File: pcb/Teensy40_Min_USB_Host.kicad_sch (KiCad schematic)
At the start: 11 parts, among them J1 USB_A, J2 Conn_01x14, J3 Conn_01x14, U1 TPD3S014, U2 Teensy4.0

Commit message: Change fuse footprint
Use the proper 0805 fuse footprint instead of the 0805 inductor footprint.
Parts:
- F1: footprint Inductor_SMD:L_0805_2012Metric -> Fuse:Fuse_0805_2012Metric
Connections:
- net at U2.3V3: now also J3.3 (Pin_3)
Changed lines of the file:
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@@
     (property "Reference" "F1" (id 0) (at 161.29 101.3165 90))
     (property "Value" "500 mA" (id 1) (at 161.29 104.0916 90))
-    (property "Footprint" "Inductor_SMD:L_0805_2012Metric" (id 2) (at 166.37 105.41 0)
+    (property "Footprint" "Fuse:Fuse_0805_2012Metric" (id 2) (at 166.37 105.41 0)
       (effects (font (size 1.27 1.27)) (justify left) hide)
     )
@@
     )
     (path "/f5825cc6-95a9-4e27-8336-4f8229fc1924"
-      (reference "F1") (unit 1) (value "500 mA") (footprint "Inductor_SMD:L_0805_2012Metric")
+      (reference "F1") (unit 1) (value "500 mA") (footprint "Fuse:Fuse_0805_2012Metric")
     )
     (path "/9ae6e37b-e62d-471c-bde9-8fd51e595ee6"

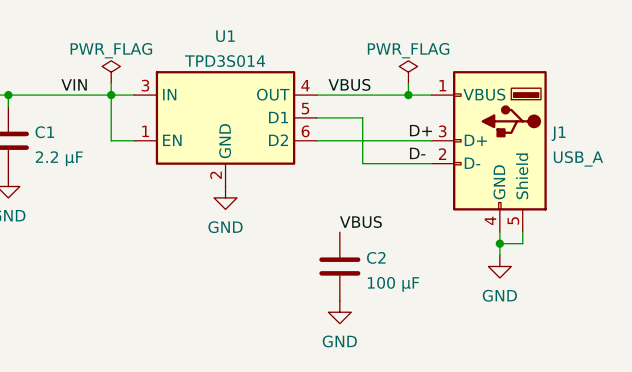
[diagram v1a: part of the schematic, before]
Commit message: Replace C2 cap with tantalum, 150 uF
Having some suspected brownout issues with rumble motors using the 100 uF ceramic cap, and I found some documentation from TI that says the USB host output capacitance should be 120 µF at a minimum.
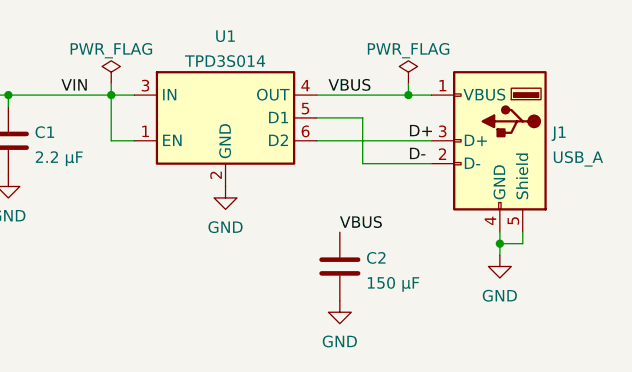
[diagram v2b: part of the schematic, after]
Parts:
- C2: value 100 µF -> 150 µF; footprint Capacitor_SMD:C_1206_3216Metric -> Capacitor_Tantalum_SMD:CP_EIA-3216-10_Kemet-I; DigiKey Product Number 13-CC1206MKX5R5BB107CT-ND -> 478-6250-1-ND; Manufacturer YAGEO -> KYOCERA AVX; Manufacturer Product Number CC1206MKX5R5BB107 -> TLNK157M006R2500
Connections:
- net at U2.3V3: now also J3.3 (Pin_3)
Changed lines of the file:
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@@
       (effects (font (size 1.27 1.27)) (justify left))
     )
-    (property "Value" "100 µF" (id 1) (at 221.361 127.5966 0)
+    (property "Value" "150 µF" (id 1) (at 221.361 127.5966 0)
       (effects (font (size 1.27 1.27)) (justify left))
     )
-    (property "Footprint" "Capacitor_SMD:C_1206_3216Metric" (id 2) (at 219.4052 129.54 0)
+    (property "Footprint" "Capacitor_Tantalum_SMD:CP_EIA-3216-10_Kemet-I" (id 2) (at 219.4052 129.54 0)
       (effects (font (size 1.27 1.27)) hide)
     )
-    (property "Datasheet" "https://www.yageo.com/upload/media/product/productsearch/datasheet/mlcc/UPY-GPHC_X5R_4V-to-50V_26.pdf" (id 3) (at 218.44 125.73 0)
+    (property "Datasheet" "https://datasheets.kyocera-avx.com/TLN_Undertab.pdf" (id 3) (at 218.44 125.73 0)
       (effects (font (size 1.27 1.27)) hide)
     )
-    (property "Description" "CAP CER 100UF 6.3V X5R 1206" (id 4) (at 218.44 125.73 0)
+    (property "Description" "CAP TANT 150UF 20% 6.3V 1206" (id 4) (at 218.44 125.73 0)
       (effects (font (size 1.27 1.27)) hide)
     )
-    (property "DigiKey Product Number" "13-CC1206MKX5R5BB107CT-ND" (id 5) (at 218.44 125.73 0)
+    (property "DigiKey Product Number" "478-6250-1-ND" (id 5) (at 218.44 125.73 0)
       (effects (font (size 1.27 1.27)) hide)
     )
-    (property "Manufacturer" "YAGEO" (id 6) (at 218.44 125.73 0)
+    (property "Manufacturer" "KYOCERA AVX" (id 6) (at 218.44 125.73 0)
       (effects (font (size 1.27 1.27)) hide)
     )
-    (property "Manufacturer Product Number" "CC1206MKX5R5BB107" (id 7) (at 218.44 125.73 0)
+    (property "Manufacturer Product Number" "TLNK157M006R2500" (id 7) (at 218.44 125.73 0)
       (effects (font (size 1.27 1.27)) hide)
     )
@@
     )
     (path "/eb66ee31-9e4d-4772-a4e6-76ee3a23c3dc"
-      (reference "C2") (unit 1) (value "100 µF") (footprint "Capacitor_SMD:C_1206_3216Metric")
+      (reference "C2") (unit 1) (value "150 µF") (footprint "Capacitor_Tantalum_SMD:CP_EIA-3216-10_Kemet-I")
     )
     (path "/f5825cc6-95a9-4e27-8336-4f8229fc1924"

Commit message: Update Teensy schematic symbol from lib
I forgot to update the schematic after updating the library. Committing now to satisfy the ERC check.
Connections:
- net at U2.3V3: now also J3.3 (Pin_3)

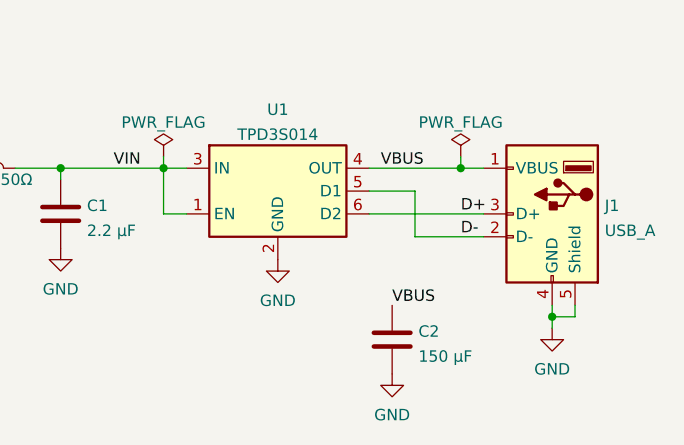
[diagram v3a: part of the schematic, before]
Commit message: Add VBUS label to schematic
Better than using a local label standalone.
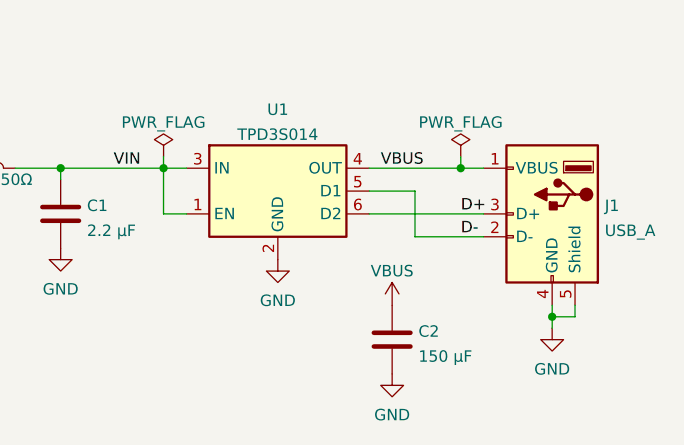
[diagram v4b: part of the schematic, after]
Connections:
- net at U2.3V3: now also J3.3 (Pin_3)
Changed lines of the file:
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@@
-    (effects (font (size 1.27 1.27)) (justify left bottom))
-  )
-  (label "VBUS" (at 218.44 121.92 0)
     (effects (font (size 1.27 1.27)) (justify left bottom))
   )
@@
     )
     (property "Datasheet" "" (id 3) (at 43.18 60.96 0)
+      (effects (font (size 1.27 1.27)) hide)
+    )
+    (pin "1")
+  )
+  (symbol (lib_id "power:VBUS") (at 218.44 121.92 0) (unit 1)
+    (in_bom yes) (on_board yes)
+    (property "Reference" "#PWR0111" (id 0) (at 218.44 125.73 0)
+      (effects (font (size 1.27 1.27)) hide)
+    )
+    (property "Value" "VBUS" (id 1) (at 218.44 118.11 0))
+    (property "Footprint" "" (id 2) (at 218.44 121.92 0)
+      (effects (font (size 1.27 1.27)) hide)
+    )
+    (property "Datasheet" "" (id 3) (at 218.44 121.92 0)
       (effects (font (size 1.27 1.27)) hide)
     )
@@
       (reference "#PWR0110") (unit 1) (value "GND") (footprint "")
     )
+    (path "/293a4c55-6604-4fbb-9af9-66b46d725551"
+      (reference "#PWR0111") (unit 1) (value "VBUS") (footprint "")
+    )
     (path "/0359c70a-e44f-4e0f-8034-bf0207c3516a"

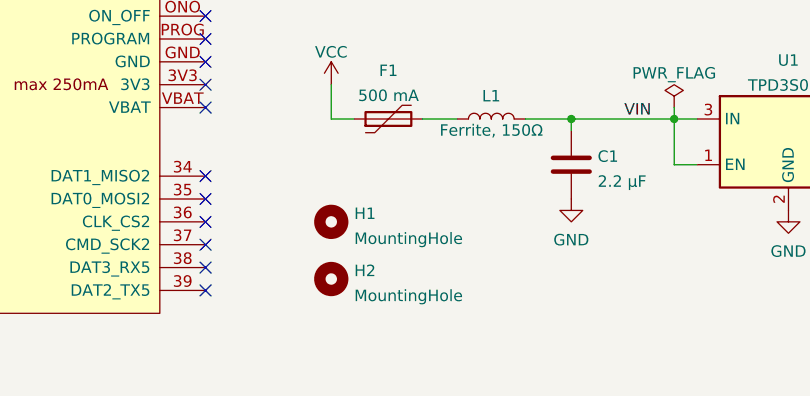
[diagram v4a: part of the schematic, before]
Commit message: Remove H2 mounting hole
This semi-circle is now part of the board outline, and the radius (1.6 mm) is large enough for most board houses that a separate drill is not needed.
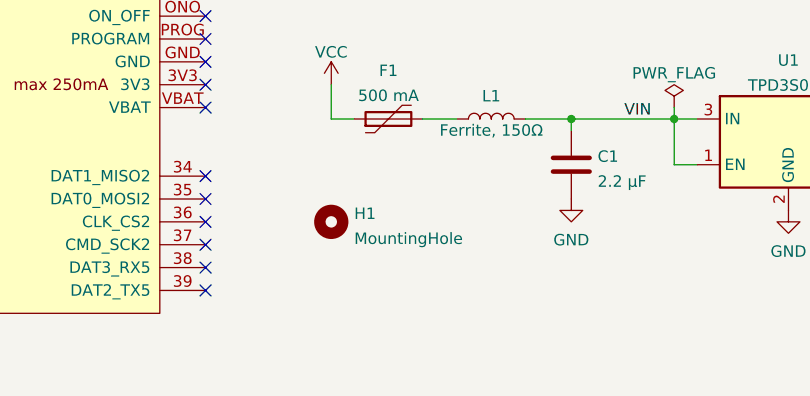
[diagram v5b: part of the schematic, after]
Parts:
- removed H2: MountingHole, Teensy40_Min_USB_Host:MountingHole_3.2mm, symbol Mechanical:MountingHole
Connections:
- net at U2.3V3: now also J3.3 (Pin_3)
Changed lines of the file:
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@@
     (pin "9")
-  )
-  (symbol (lib_id "Mechanical:MountingHole") (at 154.94 124.46 0) (unit 1)
-    (in_bom no) (on_board yes) (fields_autoplaced)
-    (property "Reference" "H2" (id 0) (at 157.48 123.5515 0)
-      (effects (font (size 1.27 1.27)) (justify left))
-    )
-    (property "Value" "MountingHole" (id 1) (at 157.48 126.3266 0)
-      (effects (font (size 1.27 1.27)) (justify left))
-    )
-    (property "Footprint" "Teensy40_Min_USB_Host:MountingHole_3.2mm" (id 2) (at 154.94 124.46 0)
-      (effects (font (size 1.27 1.27)) hide)
-    )
-    (property "Datasheet" "~" (id 3) (at 154.94 124.46 0)
-      (effects (font (size 1.27 1.27)) hide)
-    )
-    (property "Description" "~" (id 4) (at 154.94 124.46 0)
-      (effects (font (size 1.27 1.27)) hide)
-    )
-    (property "DigiKey Product Number" "~" (id 5) (at 154.94 124.46 0)
-      (effects (font (size 1.27 1.27)) hide)
-    )
-    (property "Manufacturer" "~" (id 6) (at 154.94 124.46 0)
-      (effects (font (size 1.27 1.27)) hide)
-    )
-    (property "Manufacturer Product Number" "~" (id 7) (at 154.94 124.46 0)
-      (effects (font (size 1.27 1.27)) hide)
-    )
   )
   (symbol (lib_id "Device:C") (at 218.44 125.73 0) (unit 1)
@@
       (reference "H1") (unit 1) (value "MountingHole") (footprint "Teensy40_Min_USB_Host:MountingHole_3.2mm")
     )
-    (path "/d6d7e84f-f030-406a-bc13-5b00e8372e3d"
-      (reference "H2") (unit 1) (value "MountingHole") (footprint "Teensy40_Min_USB_Host:MountingHole_3.2mm")
-    )
     (path "/c245aea9-4ca3-4a5d-88de-97c0caac9f8d"
